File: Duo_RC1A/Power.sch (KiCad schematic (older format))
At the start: 29 parts, among them U2 MC7805, U3 NCP1117DT33G

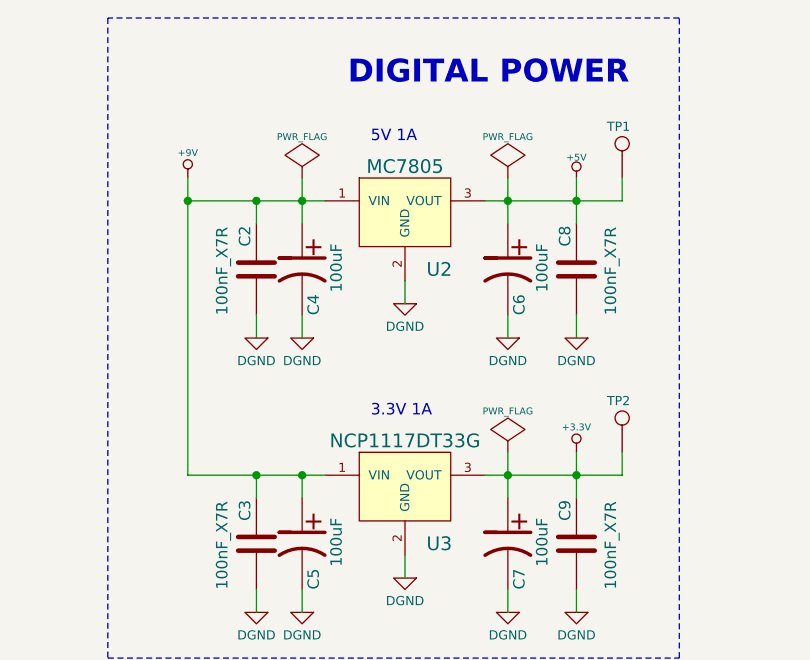
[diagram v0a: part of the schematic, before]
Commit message: PCB dimensions and group placement of all footprints on both BottomBoard and TopBoard layouts.
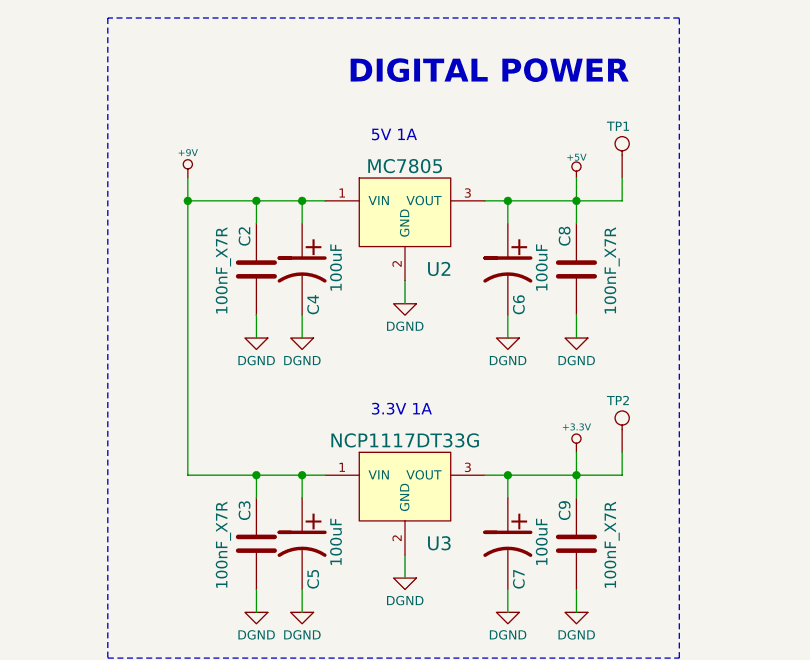
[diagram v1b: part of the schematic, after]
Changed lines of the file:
@@
-$EndComp
-$Comp
-L PWR_FLAG #FLG035
-U 1 1 537BBEC3
-P 5150 1450
-F 0 "#FLG035" H 5150 1545 30  0001 C CNN
-F 1 "PWR_FLAG" H 5150 1630 30  0000 C CNN
-F 2 "~" H 5150 1450 60  0000 C CNN
-F 3 "~" H 5150 1450 60  0000 C CNN
-	1    5150 1450
-	-1   0    0    -1
 $EndComp
 $Comp
@@
 $EndComp
 $Comp
-L DGND #PWR036
+L DGND #PWR035
 U 1 1 537BBEE3
 P 5150 3350
-F 0 "#PWR036" H 5150 3350 40  0001 C CNN
+F 0 "#PWR035" H 5150 3350 40  0001 C CNN
 F 1 "DGND" H 5150 3250 40  0000 C CNN
 F 2 "~" H 5150 3350 60  0000 C CNN
@@
 $EndComp
 $Comp
-L DGND #PWR037
+L DGND #PWR036
 U 1 1 537BBEE5
 P 5150 2150
-F 0 "#PWR037" H 5150 2150 40  0001 C CNN
+F 0 "#PWR036" H 5150 2150 40  0001 C CNN
 F 1 "DGND" H 5150 2050 40  0000 C CNN
 F 2 "~" H 5150 2150 60  0000 C CNN
@@
 $EndComp
 $Comp
-L DGND #PWR038
+L DGND #PWR037
 U 1 1 537BBEE6
 P 5600 2000
-F 0 "#PWR038" H 5600 2000 40  0001 C CNN
+F 0 "#PWR037" H 5600 2000 40  0001 C CNN
 F 1 "DGND" H 5600 1900 40  0000 C CNN
 F 2 "~" H 5600 2000 60  0000 C CNN
@@
 $EndComp
 $Comp
-L DGND #PWR039
+L DGND #PWR038
 U 1 1 537BBEE7
 P 5600 3200
-F 0 "#PWR039" H 5600 3200 40  0001 C CNN
+F 0 "#PWR038" H 5600 3200 40  0001 C CNN
 F 1 "DGND" H 5600 3100 40  0000 C CNN
 F 2 "~" H 5600 3200 60  0000 C CNN
@@
 $EndComp
 $Comp
-L DGND #PWR040
+L DGND #PWR039
 U 1 1 537BBEE9
 P 6050 2150
-F 0 "#PWR040" H 6050 2150 40  0001 C CNN
+F 0 "#PWR039" H 6050 2150 40  0001 C CNN
 F 1 "DGND" H 6050 2050 40  0000 C CNN
 F 2 "~" H 6050 2150 60  0000 C CNN
@@
 $EndComp
 $Comp
-L DGND #PWR041
+L DGND #PWR040
 U 1 1 537BBEEB
 P 6050 3350
-F 0 "#PWR041" H 6050 3350 40  0001 C CNN
+F 0 "#PWR040" H 6050 3350 40  0001 C CNN
 F 1 "DGND" H 6050 3250 40  0000 C CNN
 F 2 "~" H 6050 3350 60  0000 C CNN
@@
 $EndComp
 $Comp
-L DGND #PWR042
+L DGND #PWR041
 U 1 1 537BBEED
 P 6350 2150
-F 0 "#PWR042" H 6350 2150 40  0001 C CNN
+F 0 "#PWR041" H 6350 2150 40  0001 C CNN
 F 1 "DGND" H 6350 2050 40  0000 C CNN
 F 2 "~" H 6350 2150 60  0000 C CNN
@@
 $EndComp
 $Comp
-L DGND #PWR043
+L DGND #PWR042
 U 1 1 537BBEEF
 P 6350 3350
-F 0 "#PWR043" H 6350 3350 40  0001 C CNN
+F 0 "#PWR042" H 6350 3350 40  0001 C CNN
 F 1 "DGND" H 6350 3250 40  0000 C CNN
 F 2 "~" H 6350 3350 60  0000 C CNN
@@
 $EndComp
 $Comp
-L +3.3V #PWR044
+L +3.3V #PWR043
 U 1 1 537BBEF0
 P 6350 2650
-F 0 "#PWR044" H 6350 2610 30  0001 C CNN
+F 0 "#PWR043" H 6350 2610 30  0001 C CNN
 F 1 "+3.3V" H 6350 2760 30  0000 C CNN
 F 2 "" H 6350 2650 60  0000 C CNN
@@
 $EndComp
 $Comp
-L +5V #PWR045
+L +5V #PWR044
 U 1 1 537BBEF1
 P 6350 1450
-F 0 "#PWR045" H 6350 1540 20  0001 C CNN
+F 0 "#PWR044" H 6350 1540 20  0001 C CNN
 F 1 "+5V" H 6350 1540 30  0000 C CNN
 F 2 "~" H 6350 1450 60  0000 C CNN
@@
 	1    6350 1450
 	1    0    0    -1
-$EndComp
-$Comp
-L PWR_FLAG #FLG046
-U 1 1 537BBEF2
-P 6050 1450
-F 0 "#FLG046" H 6050 1545 30  0001 C CNN
-F 1 "PWR_FLAG" H 6050 1630 30  0000 C CNN
-F 2 "~" H 6050 1450 60  0000 C CNN
-F 3 "~" H 6050 1450 60  0000 C CNN
-	1    6050 1450
-	-1   0    0    -1
-$EndComp
-$Comp
-L PWR_FLAG #FLG047
-U 1 1 537BBEF3
-P 6050 2650
-F 0 "#FLG047" H 6050 2745 30  0001 C CNN
-F 1 "PWR_FLAG" H 6050 2830 30  0000 C CNN
-F 2 "~" H 6050 2650 60  0000 C CNN
-F 3 "~" H 6050 2650 60  0000 C CNN
-	1    6050 2650
-	-1   0    0    -1
 $EndComp
 $Comp
@@
 $EndComp
 $Comp
-L +9VA #PWR048
+L +9VA #PWR045
 U 1 1 537BFDA4
 P 3250 4350
-F 0 "#PWR048" H 3250 4320 20  0001 C CNN
+F 0 "#PWR045" H 3250 4320 20  0001 C CNN
 F 1 "+9VA" H 3250 4460 30  0000 C CNN
 F 2 "" H 3250 4350 60  0000 C CNN
@@
 $EndComp
 $Comp
-L DGND #PWR049
+L DGND #PWR046
 U 1 1 537C0469
 P 4950 3350
-F 0 "#PWR049" H 4950 3350 40  0001 C CNN
+F 0 "#PWR046" H 4950 3350 40  0001 C CNN
 F 1 "DGND" H 4950 3250 40  0000 C CNN
 F 2 "~" H 4950 3350 60  0000 C CNN
@@
 Wire Wire Line
 	5150 2050 5150 2150
-Wire Wire Line
-	5150 1450 5150 1650
 Connection ~ 5150 1550
 Wire Wire Line
@@
 	5950 1550 6550 1550
 Wire Wire Line
-	6050 1450 6050 1650
-Wire Wire Line
 	5950 2750 6550 2750
-Wire Wire Line
-	6050 2650 6050 2850
 Wire Wire Line
 	6350 2150 6350 2050
@@
 $EndComp
 $Comp
-L DGND #PWR050
+L DGND #PWR047
 U 1 1 537C0568
 P 4950 2150
-F 0 "#PWR050" H 4950 2150 40  0001 C CNN
+F 0 "#PWR047" H 4950 2150 40  0001 C CNN
 F 1 "DGND" H 4950 2050 40  0000 C CNN
 F 2 "~" H 4950 2150 60  0000 C CNN
@@
 Wire Notes Line
 	2850 6400 2850 3800
+Wire Wire Line
+	6050 1550 6050 1650
+Wire Wire Line
+	6050 2750 6050 2850
+Wire Wire Line
+	5150 1550 5150 1650
 $EndSCHEMATC

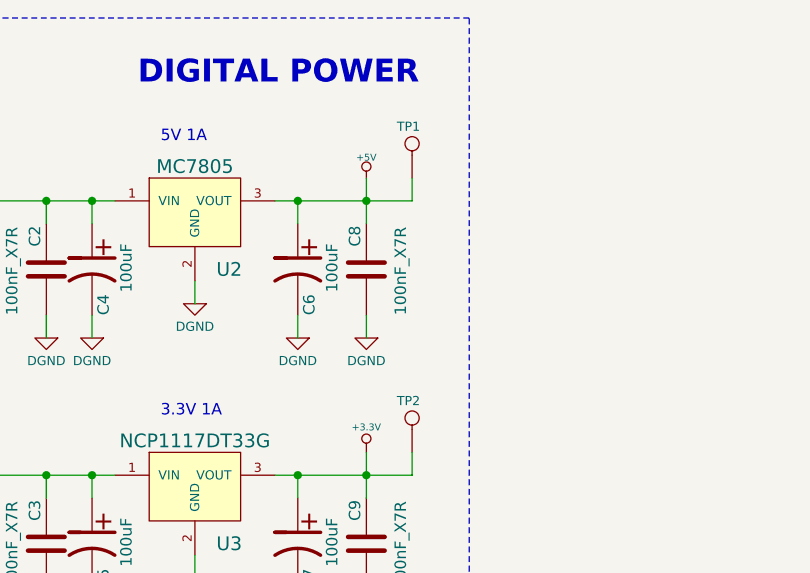
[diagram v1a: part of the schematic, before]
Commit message: Working on the BottomBoard layout. Moved the ITEAD Coreboard to the board left side so there is more space for the linear regulators. Stopped on the USB OTG and USB Host layout.
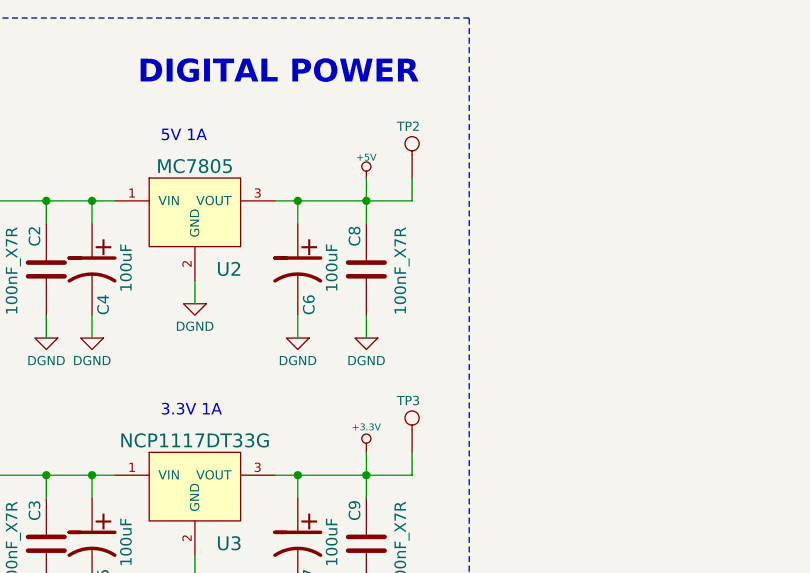
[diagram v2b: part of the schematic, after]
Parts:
- renumbered TP1 to TP2, TP2 to TP3
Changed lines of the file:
@@
 $EndDescr
 $Comp
-L AGND #PWR010
+L AGND #PWR014
 U 1 1 537BBE83
 P 3600 5650
-F 0 "#PWR010" H 3600 5650 40  0001 C CNN
+F 0 "#PWR014" H 3600 5650 40  0001 C CNN
 F 1 "AGND" H 3600 5580 50  0000 C CNN
 F 2 "~" H 3600 5650 60  0000 C CNN
@@
 $EndComp
 $Comp
-L PWR_FLAG #FLG011
+L PWR_FLAG #FLG015
 U 1 1 537BBE88
 P 8150 4350
-F 0 "#FLG011" H 8150 4445 30  0001 C CNN
+F 0 "#FLG015" H 8150 4445 30  0001 C CNN
 F 1 "PWR_FLAG" H 8150 4530 30  0000 C CNN
 F 2 "~" H 8150 4350 60  0000 C CNN
@@
 $EndComp
 $Comp
-L +5VA #PWR012
+L +5VA #PWR016
 U 1 1 537BBE89
 P 7900 4350
-F 0 "#PWR012" H 7900 4480 20  0001 C CNN
+F 0 "#PWR016" H 7900 4480 20  0001 C CNN
 F 1 "+5VA" H 7900 4450 30  0000 C CNN
 F 2 "~" H 7900 4350 60  0000 C CNN
@@
 $EndComp
 $Comp
-L DGND #PWR013
+L DGND #PWR017
 U 1 1 537BBE8A
 P 3300 5650
-F 0 "#PWR013" H 3300 5650 40  0001 C CNN
+F 0 "#PWR017" H 3300 5650 40  0001 C CNN
 F 1 "DGND" H 3300 5580 40  0000 C CNN
 F 2 "~" H 3300 5650 60  0000 C CNN
@@
 $EndComp
 $Comp
-L AGND #PWR014
+L AGND #PWR018
 U 1 1 537BBE8B
 P 6400 4900
-F 0 "#PWR014" H 6400 4900 40  0001 C CNN
+F 0 "#PWR018" H 6400 4900 40  0001 C CNN
 F 1 "AGND" H 6400 4830 50  0000 C CNN
 F 2 "~" H 6400 4900 60  0000 C CNN
@@
 $EndComp
 $Comp
-L +3.3VA #PWR015
+L +3.3VA #PWR019
 U 1 1 537BBE8C
 P 7900 5450
-F 0 "#PWR015" H 7900 5410 30  0001 C CNN
+F 0 "#PWR019" H 7900 5410 30  0001 C CNN
 F 1 "+3.3VA" H 7900 5560 30  0000 C CNN
 F 2 "~" H 7900 5450 60  0000 C CNN
@@
 $EndComp
 $Comp
-L AGND #PWR016
+L AGND #PWR020
 U 1 1 537BBE8D
 P 5450 6150
-F 0 "#PWR016" H 5450 6150 40  0001 C CNN
+F 0 "#PWR020" H 5450 6150 40  0001 C CNN
 F 1 "AGND" H 5450 6080 50  0000 C CNN
 F 2 "~" H 5450 6150 60  0000 C CNN
@@
 $EndComp
 $Comp
-L VCC_AMP_AUDIO #PWR017
+L VCC_AMP_AUDIO #PWR021
 U 1 1 537BBE8E
 P 5750 4350
-F 0 "#PWR017" H 5750 4450 30  0001 C CNN
+F 0 "#PWR021" H 5750 4450 30  0001 C CNN
 F 1 "VCC_AMP_AUDIO" H 5750 4450 30  0000 C CNN
 F 2 "~" H 5750 4350 60  0000 C CNN
@@
 $EndComp
 $Comp
-L AGND #PWR018
+L AGND #PWR022
 U 1 1 537BBE94
 P 5750 6150
-F 0 "#PWR018" H 5750 6150 40  0001 C CNN
+F 0 "#PWR022" H 5750 6150 40  0001 C CNN
 F 1 "AGND" H 5750 6080 50  0000 C CNN
 F 2 "~" H 5750 6150 60  0000 C CNN
@@
 $EndComp
 $Comp
-L AGND #PWR019
+L AGND #PWR023
 U 1 1 537BBE99
 P 4400 5050
-F 0 "#PWR019" H 4400 5050 40  0001 C CNN
+F 0 "#PWR023" H 4400 5050 40  0001 C CNN
 F 1 "AGND" H 4400 4980 50  0000 C CNN
 F 2 "~" H 4400 5050 60  0000 C CNN
@@
 $EndComp
 $Comp
-L AGND #PWR020
+L AGND #PWR024
 U 1 1 537BBE9B
 P 4100 4650
-F 0 "#PWR020" H 4100 4650 40  0001 C CNN
+F 0 "#PWR024" H 4100 4650 40  0001 C CNN
 F 1 "AGND" H 4100 4580 50  0000 C CNN
 F 2 "~" H 4100 4650 60  0000 C CNN
@@
 $EndComp
 $Comp
-L AGND #PWR021
+L AGND #PWR025
 U 1 1 537BBE9C
 P 3900 4650
-F 0 "#PWR021" H 3900 4650 40  0001 C CNN
+F 0 "#PWR025" H 3900 4650 40  0001 C CNN
 F 1 "AGND" H 3900 4580 50  0000 C CNN
 F 2 "~" H 3900 4650 60  0000 C CNN
@@
 $EndComp
 $Comp
-L AGND #PWR022
+L AGND #PWR026
 U 1 1 537BBE9E
 P 4750 5050
-F 0 "#PWR022" H 4750 5050 40  0001 C CNN
+F 0 "#PWR026" H 4750 5050 40  0001 C CNN
 F 1 "AGND" H 4750 4980 50  0000 C CNN
 F 2 "~" H 4750 5050 60  0000 C CNN
@@
 $EndComp
 $Comp
-L AGND #PWR023
+L AGND #PWR027
 U 1 1 537BBE9F
 P 5100 5050
-F 0 "#PWR023" H 5100 5050 40  0001 C CNN
+F 0 "#PWR027" H 5100 5050 40  0001 C CNN
 F 1 "AGND" H 5100 4980 50  0000 C CNN
 F 2 "~" H 5100 5050 60  0000 C CNN
@@
 $EndComp
 $Comp
-L AGND #PWR024
+L AGND #PWR028
 U 1 1 537BBEA0
 P 5450 5050
-F 0 "#PWR024" H 5450 5050 40  0001 C CNN
+F 0 "#PWR028" H 5450 5050 40  0001 C CNN
 F 1 "AGND" H 5450 4980 50  0000 C CNN
 F 2 "~" H 5450 5050 60  0000 C CNN
@@
 $EndComp
 $Comp
-L AGND #PWR025
+L AGND #PWR029
 U 1 1 537BBEA2
 P 7200 5050
-F 0 "#PWR025" H 7200 5050 40  0001 C CNN
+F 0 "#PWR029" H 7200 5050 40  0001 C CNN
 F 1 "AGND" H 7200 4980 50  0000 C CNN
 F 2 "~" H 7200 5050 60  0000 C CNN
@@
 $EndComp
 $Comp
-L AGND #PWR026
+L AGND #PWR030
 U 1 1 537BBEA3
 P 6850 5050
-F 0 "#PWR026" H 6850 5050 40  0001 C CNN
+F 0 "#PWR030" H 6850 5050 40  0001 C CNN
 F 1 "AGND" H 6850 4980 50  0000 C CNN
 F 2 "~" H 6850 5050 60  0000 C CNN
@@
 $EndComp
 $Comp
-L PWR_FLAG #FLG027
+L PWR_FLAG #FLG031
 U 1 1 537BBEA5
 P 8150 5450
-F 0 "#FLG027" H 8150 5545 30  0001 C CNN
+F 0 "#FLG031" H 8150 5545 30  0001 C CNN
 F 1 "PWR_FLAG" H 8150 5630 30  0000 C CNN
 F 2 "~" H 8150 5450 60  0000 C CNN
@@
 3.3V 1A
 $Comp
-L AGND #PWR028
+L AGND #PWR032
 U 1 1 537BBEA6
 P 7200 6150
-F 0 "#PWR028" H 7200 6150 40  0001 C CNN
+F 0 "#PWR032" H 7200 6150 40  0001 C CNN
 F 1 "AGND" H 7200 6080 50  0000 C CNN
 F 2 "~" H 7200 6150 60  0000 C CNN
@@
 $EndComp
 $Comp
-L AGND #PWR029
+L AGND #PWR033
 U 1 1 537BBEA7
 P 6850 6150
-F 0 "#PWR029" H 6850 6150 40  0001 C CNN
+F 0 "#PWR033" H 6850 6150 40  0001 C CNN
 F 1 "AGND" H 6850 6080 50  0000 C CNN
 F 2 "~" H 6850 6150 60  0000 C CNN
@@
 $EndComp
 $Comp
-L PWR_FLAG #FLG030
+L PWR_FLAG #FLG034
 U 1 1 537BBEAA
 P 5450 4350
-F 0 "#FLG030" H 5450 4445 30  0001 C CNN
+F 0 "#FLG034" H 5450 4445 30  0001 C CNN
 F 1 "PWR_FLAG" H 5450 4530 30  0000 C CNN
 F 2 "" H 5450 4350 60  0000 C CNN
@@
 $EndComp
 $Comp
-L AGND #PWR031
+L AGND #PWR035
 U 1 1 537BBEAB
 P 6400 6000
-F 0 "#PWR031" H 6400 6000 40  0001 C CNN
+F 0 "#PWR035" H 6400 6000 40  0001 C CNN
 F 1 "AGND" H 6400 5930 50  0000 C CNN
 F 2 "~" H 6400 6000 60  0000 C CNN
@@
 $EndComp
 $Comp
-L DGND #PWR032
+L DGND #PWR036
 U 1 1 537BBEAD
 P 3250 5050
-F 0 "#PWR032" H 3250 5050 40  0001 C CNN
+F 0 "#PWR036" H 3250 5050 40  0001 C CNN
 F 1 "DGND" H 3250 4980 40  0000 C CNN
 F 2 "~" H 3250 5050 60  0000 C CNN
@@
 $EndComp
 $Comp
-L DGND #PWR033
+L DGND #PWR037
 U 1 1 537BBEAE
 P 3600 5050
-F 0 "#PWR033" H 3600 5050 40  0001 C CNN
+F 0 "#PWR037" H 3600 5050 40  0001 C CNN
 F 1 "DGND" H 3600 4980 40  0000 C CNN
 F 2 "~" H 3600 5050 60  0000 C CNN
@@
 $EndComp
 $Comp
-L +9V #PWR034
+L +9V #PWR038
 U 1 1 537BBEC2
 P 4650 1450
-F 0 "#PWR034" H 4650 1420 20  0001 C CNN
+F 0 "#PWR038" H 4650 1420 20  0001 C CNN
 F 1 "+9V" H 4650 1560 30  0000 C CNN
 F 2 "~" H 4650 1450 60  0000 C CNN
@@
 $EndComp
 $Comp
-L DGND #PWR035
+L DGND #PWR039
 U 1 1 537BBEE3
 P 5150 3350
-F 0 "#PWR035" H 5150 3350 40  0001 C CNN
+F 0 "#PWR039" H 5150 3350 40  0001 C CNN
 F 1 "DGND" H 5150 3250 40  0000 C CNN
 F 2 "~" H 5150 3350 60  0000 C CNN
@@
 $EndComp
 $Comp
-L DGND #PWR036
+L DGND #PWR040
 U 1 1 537BBEE5
 P 5150 2150
-F 0 "#PWR036" H 5150 2150 40  0001 C CNN
+F 0 "#PWR040" H 5150 2150 40  0001 C CNN
 F 1 "DGND" H 5150 2050 40  0000 C CNN
 F 2 "~" H 5150 2150 60  0000 C CNN
@@
 $EndComp
 $Comp
-L DGND #PWR037
+L DGND #PWR041
 U 1 1 537BBEE6
 P 5600 2000
-F 0 "#PWR037" H 5600 2000 40  0001 C CNN
+F 0 "#PWR041" H 5600 2000 40  0001 C CNN
 F 1 "DGND" H 5600 1900 40  0000 C CNN
 F 2 "~" H 5600 2000 60  0000 C CNN
@@
 $EndComp
 $Comp
-L DGND #PWR038
+L DGND #PWR042
 U 1 1 537BBEE7
 P 5600 3200
-F 0 "#PWR038" H 5600 3200 40  0001 C CNN
+F 0 "#PWR042" H 5600 3200 40  0001 C CNN
 F 1 "DGND" H 5600 3100 40  0000 C CNN
 F 2 "~" H 5600 3200 60  0000 C CNN
@@
 $EndComp
 $Comp
-L DGND #PWR039
+L DGND #PWR043
 U 1 1 537BBEE9
 P 6050 2150
-F 0 "#PWR039" H 6050 2150 40  0001 C CNN
+F 0 "#PWR043" H 6050 2150 40  0001 C CNN
 F 1 "DGND" H 6050 2050 40  0000 C CNN
 F 2 "~" H 6050 2150 60  0000 C CNN
@@
 $EndComp
 $Comp
-L DGND #PWR040
+L DGND #PWR044
 U 1 1 537BBEEB
 P 6050 3350
-F 0 "#PWR040" H 6050 3350 40  0001 C CNN
+F 0 "#PWR044" H 6050 3350 40  0001 C CNN
 F 1 "DGND" H 6050 3250 40  0000 C CNN
 F 2 "~" H 6050 3350 60  0000 C CNN
@@
 $EndComp
 $Comp
-L DGND #PWR041
+L DGND #PWR045
 U 1 1 537BBEED
 P 6350 2150
-F 0 "#PWR041" H 6350 2150 40  0001 C CNN
+F 0 "#PWR045" H 6350 2150 40  0001 C CNN
 F 1 "DGND" H 6350 2050 40  0000 C CNN
 F 2 "~" H 6350 2150 60  0000 C CNN
@@
 $EndComp
 $Comp
-L DGND #PWR042
+L DGND #PWR046
 U 1 1 537BBEEF
 P 6350 3350
-F 0 "#PWR042" H 6350 3350 40  0001 C CNN
+F 0 "#PWR046" H 6350 3350 40  0001 C CNN
 F 1 "DGND" H 6350 3250 40  0000 C CNN
 F 2 "~" H 6350 3350 60  0000 C CNN
@@
 $EndComp
 $Comp
-L +3.3V #PWR043
+L +3.3V #PWR047
 U 1 1 537BBEF0
 P 6350 2650
-F 0 "#PWR043" H 6350 2610 30  0001 C CNN
+F 0 "#PWR047" H 6350 2610 30  0001 C CNN
 F 1 "+3.3V" H 6350 2760 30  0000 C CNN
 F 2 "" H 6350 2650 60  0000 C CNN
@@
 $EndComp
 $Comp
-L +5V #PWR044
+L +5V #PWR048
 U 1 1 537BBEF1
 P 6350 1450
-F 0 "#PWR044" H 6350 1540 20  0001 C CNN
+F 0 "#PWR048" H 6350 1540 20  0001 C CNN
 F 1 "+5V" H 6350 1540 30  0000 C CNN
 F 2 "~" H 6350 1450 60  0000 C CNN
@@
 $EndComp
 $Comp
-L CONN_1 TP1
+L CONN_1 TP2
 U 1 1 537BBEF6
 P 6550 1300
-F 0 "TP1" V 6625 1265 40  0000 L CNN
+F 0 "TP2" V 6625 1265 40  0000 L CNN
 F 1 "TEST_POINT_1MM" H 6550 1355 30  0001 C CNN
 F 2 "Duo_Audio_HMI_RC1A:TESTPOINT_1MM" H 6550 1300 60  0001 C CNN
@@
 $EndComp
 $Comp
-L CONN_1 TP2
+L CONN_1 TP3
 U 1 1 537BBEF7
 P 6550 2500
-F 0 "TP2" V 6625 2465 40  0000 L CNN
+F 0 "TP3" V 6625 2465 40  0000 L CNN
 F 1 "TEST_POINT_1MM" H 6550 2555 30  0001 C CNN
 F 2 "Duo_Audio_HMI_RC1A:TESTPOINT_1MM" H 6550 2500 60  0001 C CNN
@@
 $EndComp
 $Comp
-L +9VA #PWR045
+L +9VA #PWR049
 U 1 1 537BFDA4
 P 3250 4350
-F 0 "#PWR045" H 3250 4320 20  0001 C CNN
+F 0 "#PWR049" H 3250 4320 20  0001 C CNN
 F 1 "+9VA" H 3250 4460 30  0000 C CNN
 F 2 "" H 3250 4350 60  0000 C CNN
@@
 $EndComp
 $Comp
-L DGND #PWR046
+L DGND #PWR050
 U 1 1 537C0469
 P 4950 3350
-F 0 "#PWR046" H 4950 3350 40  0001 C CNN
+F 0 "#PWR050" H 4950 3350 40  0001 C CNN
 F 1 "DGND" H 4950 3250 40  0000 C CNN
 F 2 "~" H 4950 3350 60  0000 C CNN
@@
 $EndComp
 $Comp
-L DGND #PWR047
+L DGND #PWR051
 U 1 1 537C0568
 P 4950 2150
-F 0 "#PWR047" H 4950 2150 40  0001 C CNN
+F 0 "#PWR051" H 4950 2150 40  0001 C CNN
 F 1 "DGND" H 4950 2050 40  0000 C CNN
 F 2 "~" H 4950 2150 60  0000 C CNN
